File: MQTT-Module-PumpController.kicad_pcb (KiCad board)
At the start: 4 copper layers, 44 x 55.9 mm, 36 parts, among them IC801 LM5060MMX_NOPB, J301 A2541WV-10P, J302 A2541WV-10P, J303 1715721, J304 A2541HWV-3P, Q801 60V 38A, U201 ATtiny1614-SS

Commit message: Updated schematic and board with adjustments, updated board.
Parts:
- removed J304: A2541HWV-3P, CJT Connectors:PinSocket_1x03_P2.54mm_Vertical_Female
- removed R202: 4.7kΩ 1/8W 1%, JLCPCB Basic:RESC2013X65N
- removed R203: 33Ω 1/8W 1%, JLCPCB Basic:RESC2013X65N
- added R205: 220Ω 1/8W 1%, JLCPCB Basic:RESC2013X65N, F.Cu at (128.1, 77.7)
- added R206: 75Ω 1/8W 1%, JLCPCB Basic:RESC2013X65N, F.Cu at (123.7, 77.7)
- R201: value 33Ω 1/8W 1% -> 330Ω 1/8W 1%
- moved R201 15.5 mm to (125.5, 93.0), turned to 180 degrees
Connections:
- J301 pad 7: /Headers/CS -> /Controller/UPDI_C
- R201 pad 1: /Controller/P_WARN -> /Controller/UPDI
- R201 pad 2: Net-(D201-A) -> /Controller/UPDI_C
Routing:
- net +3V3: track 70.7 -> 58.1 mm
- net /Controller/UPDI: track 13.2 -> 22.2 mm
- net /Controller/UDPI_C: track 5.30 -> 0.00 mm
- net /Controller/UPDI_C: track 0.00 -> 5.30 mm
- net /Controller/PMP_EN: track 6.58 -> 8.93 mm
- net GND: vias 44 -> 48

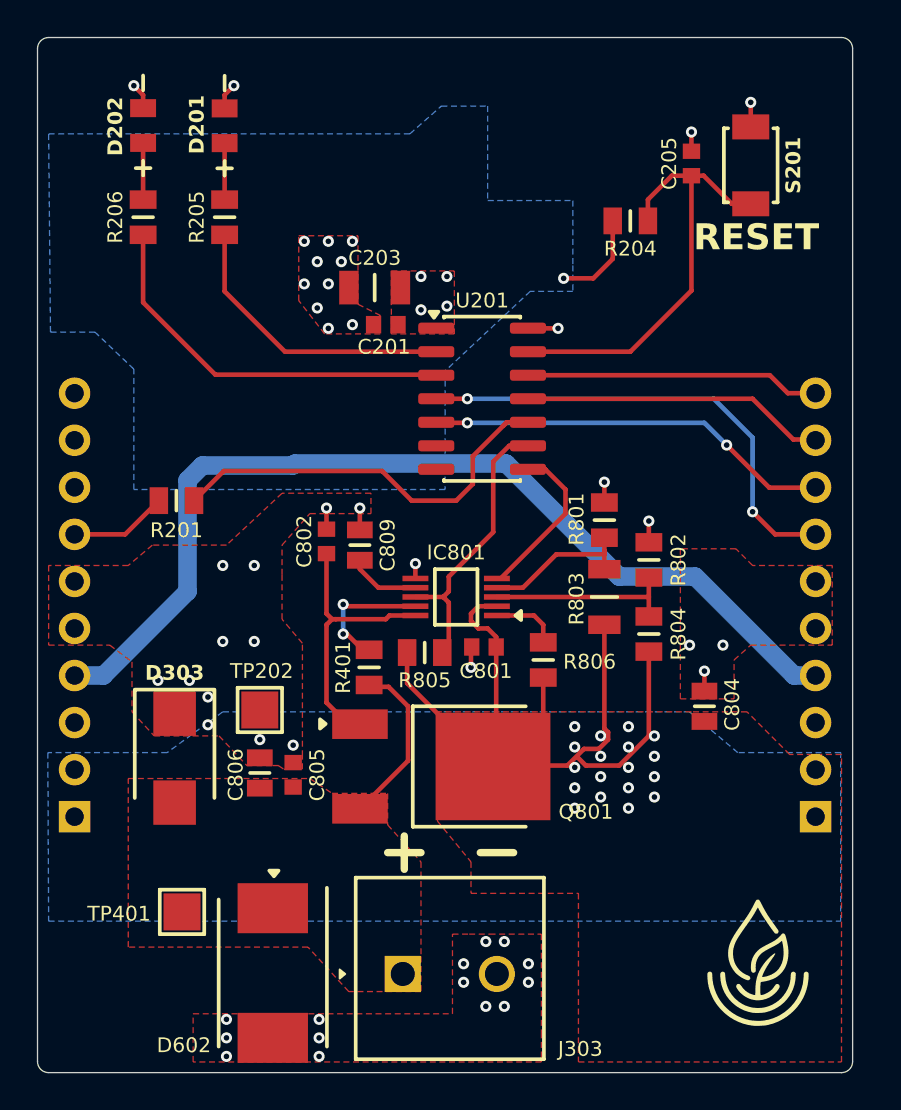
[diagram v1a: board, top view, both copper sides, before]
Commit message: Updated schematic, redesigned and included pump pressure switch. Regenerated all outputs.
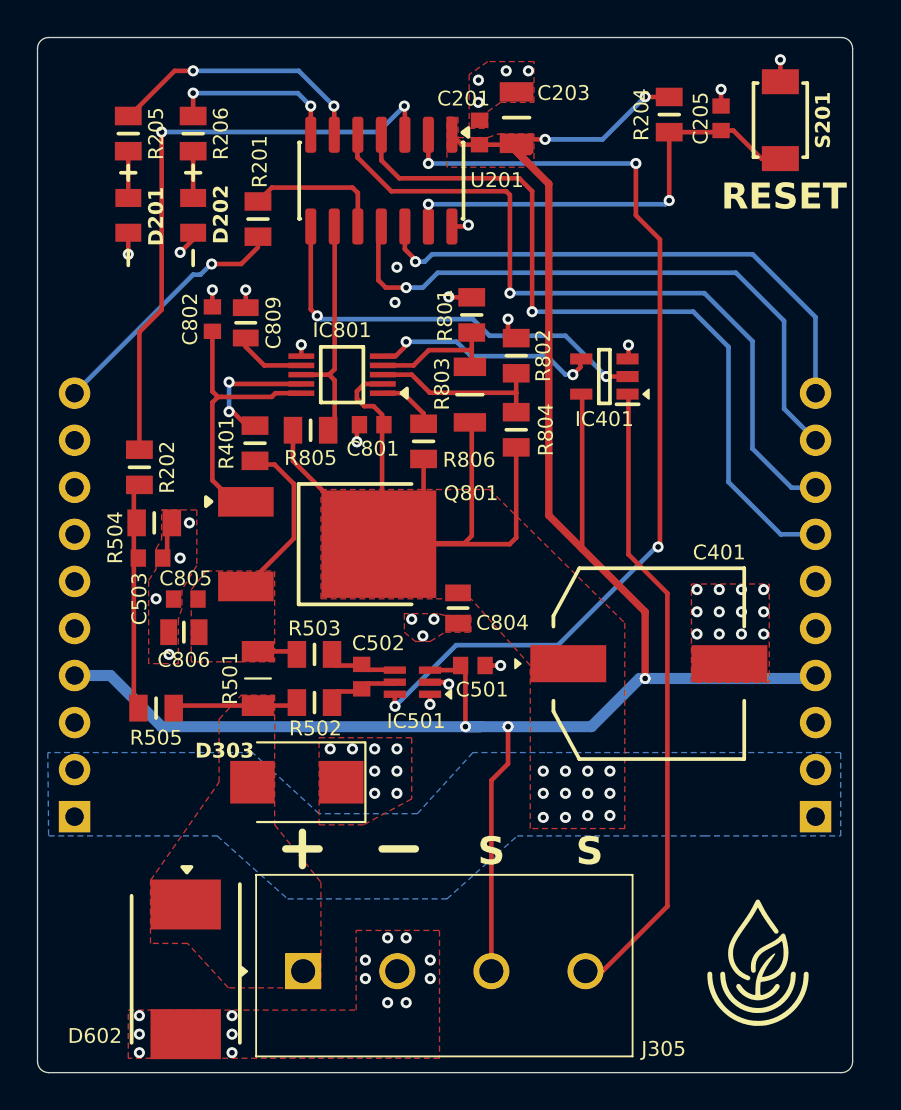
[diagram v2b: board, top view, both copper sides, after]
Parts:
- removed J303: 1715721, PHOENIX CONTACT Terminals:1715721
- removed TP202, TP401: TestPoint, TestPoint:TestPoint_Pad_2.0x2.0mm
- added C401: 470uF 20% 25V, PANASONIC Capacitors:EEEFK1V331P, F.Cu at (151.0, 101.8)
- added C501: 0.1uF 10% 50V, JLCPCB Basic:CAPC1608X90N, F.Cu at (141.5, 101.9)
- added C502: 22nF 10% 50V, JLCPCB Basic:CAPC1608X90N, F.Cu at (135.5, 102.5)
- added C503: 0.1uF 10% 50V, JLCPCB Basic:CAPC1608X90N, F.Cu at (124.1, 96.1)
- added IC401: SN74LVC1G08DBVR, TEXAS INSTRUMENTS ICs:SOT95P280X145-5N, F.Cu at (148.6, 86.3)
- added IC501: INA186A1IDCKR, TEXAS INSTRUMENTS ICs:SOT65P210X110-6N, F.Cu at (138.2, 102.8)
- added J305: 1715747, PHOENIX CONTACT Terminals:1715747, F.Cu at (132.3, 118.4)
- added R202: 1kΩ 1/8W 1%, JLCPCB Basic:RESC2013X65N, F.Cu at (123.5, 91.2)
- added R501: 20mΩ 1% 1W, VISHAY INTERTECH Resistors:R_1206_3216Metric, F.Cu at (129.9, 102.6)
- added R502: 100Ω 1/8W 1%, JLCPCB Basic:RESC2013X65N, F.Cu at (132.9, 103.9)
- added R503: 100Ω 1/8W 1%, JLCPCB Basic:RESC2013X65N, F.Cu at (132.9, 101.3)
- added R504: 24kΩ 1/8W 1%, JLCPCB Basic:RESC2013X65N, F.Cu at (124.3, 94.2)
- added R505: 100kΩ 1/8W 1%, JLCPCB Basic:RESC2013X65N, F.Cu at (124.4, 104.2)
- moved R201 15.8 mm to (129.9, 77.8), turned to -90 degrees
- moved C804 14.3 mm to (140.7, 98.8), turned to -90 degrees
- moved R401 13.6 mm to (129.7, 89.9)
- moved C802 13.5 mm to (127.4, 83.2)
- moved C809 13.5 mm to (129.2, 83.4)
- moved IC801 13.5 mm to (134.4, 86.2)
- moved Q801 13.5 mm to (138.2, 95.3)
- moved R805 13.5 mm to (132.7, 89.2)
- moved R806 13.5 mm to (138.8, 89.8)
- moved C801 13.4 mm to (136.0, 88.9)
- moved R801 13.2 mm to (141.4, 83.0)
- moved R802 13.1 mm to (143.8, 85.2)
- moved R804 13.1 mm to (143.8, 89.2)
- moved R803 13.1 mm to (141.3, 87.3)
- moved U201 13.0 mm to (136.6, 75.7), turned to -90 degrees
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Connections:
- C805 pad 1: /Headers/PMP+ -> /Pump Controller/PMP_Sense
- C806 pad 1: /Headers/PMP+ -> /Pump Controller/PMP_Sense
- IC801 pad 5: /Controller/PMP_EN -> Net-(IC401-Y)
- J301 pad 10: /Headers/MOSI -> /Controller/UPDI_C
- J301 pad 7: /Controller/UPDI_C -> /Headers/CS
- Q801 pad 3: /Headers/PMP+ -> /Pump Controller/PMP_Sense
- R401 pad 2: /Headers/PMP+ -> /Pump Controller/PMP_Sense
- U201 pad 2: /Controller/P_WARN -> /Controller/PI_SNS
- U201 pad 3: /Controller/P_ON -> /Controller/PV_SNS
- U201 pad 6: unconnected-(U201-PB3-Pad6) -> /Controller/P_WARN
- U201 pad 7: unconnected-(U201-PB2-Pad7) -> /Controller/P_ON
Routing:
- net +3V3: track 58.1 -> 116.6 mm
- net /Controller/PI_SNS: track 0.00 -> 52.3 mm, vias 0 -> 4
- net /Headers/Pressure_Sensor: track 0.00 -> 34.4 mm
- net /Controller/PV_SNS: track 0.00 -> 32.9 mm, vias 0 -> 2
- net /Controller/SNS: track 21.9 -> 39.9 mm, vias 2 -> 1
- net /Controller/SDA: track 16.5 -> 33.6 mm, vias 0 -> 1
- net /Controller/MOD: track 25.9 -> 41.3 mm, vias 2 -> 1
- net /Controller/UPDI: track 22.2 -> 7.63 mm
- net /Controller/PMP_EN: track 8.93 -> 23.1 mm, vias 0 -> 2
- net /Controller/SCL: track 16.2 -> 29.7 mm, vias 0 -> 1
- net /Controller/PV_SNS_R: track 0.00 -> 12.8 mm
- net Net-(IC401-Y): track 0.00 -> 12.5 mm, vias 0 -> 2
- net /Controller/P_ON: track 21.1 -> 9.43 mm, vias 0 -> 2
- net /Pump Controller/PMP_Sense: track 0.00 -> 11.4 mm
- net /Controller/UPDI_C: track 5.30 -> 13.2 mm, vias 0 -> 1
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- added copper zone on F.Cu, net /Pump Controller/PMP_Sense
- removed copper zone on B.Cu, net +3V3
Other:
- board text added: "Pressure Sensor"
- board text added: "Pump - / +"
- board text added: "S"

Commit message: Added pull downs on enable lines and regenerated outputs.
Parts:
- added R402: 10kΩ 1/8W 1%, JLCPCB Basic:RESC2013X65N, F.Cu at (152.4, 89.6)
- added R403: 10kΩ 1/8W 1%, JLCPCB Basic:RESC2013X65N, F.Cu at (152.4, 85.1)
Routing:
- net /Headers/Pressure_Sensor: track 34.4 -> 38.4 mm
- net /Controller/PMP_EN: track 23.1 -> 26.8 mm
- net /Controller/PI_SNS: track 52.3 -> 55.9 mm
- net GND: track 16.7 -> 19.3 mm, vias 62 -> 64

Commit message: Swapped 12v pull up to 3.3v pull up and added 0.1uf cap to AND, then regenerated outputs.
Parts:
- removed R805: 4.7kΩ 1/8W 1%, JLCPCB Basic:RESC2013X65N
- added C402: 0.1uF 10% 50V, JLCPCB Basic:CAPC1608X90N, F.Cu at (148.1, 89.0)
- added R404: 1kΩ 1/8W 1%, JLCPCB Basic:RESC2013X65N, F.Cu at (135.0, 83.1)
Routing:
- net +3V3: track 116.6 -> 134.5 mm, vias 5 -> 6
- net +12V: track 48.6 -> 40.6 mm
- net /Controller/PMP_Status: track 12.9 -> 9.63 mm
- net GND: track 19.3 -> 20.4 mm, vias 64 -> 65

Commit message: Updated layout, and regenerated outputs.
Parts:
- removed R201: 330Ω 1/8W 1%, JLCPCB Basic:RESC2013X65N
- added J303: A2541HWV-3P, CJT Connectors:PinSocket_1x03_P2.54mm_Vertical_Female, F.Cu at (159.6, 77.6)
- added R203: 470Ω 1/8W 1%, JLCPCB Basic:RESC2013X65N, F.Cu at (130.1, 73.9)
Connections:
- J301 pad 10: /Controller/UPDI_C -> /Headers/MOSI
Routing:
- net /Controller/UPDI_C: track 13.2 -> 32.9 mm, vias 1 -> 0
- net +3V3: track 134.5 -> 150.8 mm
- net /Controller/RESET: track 24.3 -> 23.3 mm
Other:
- board text added: "G"
- board text added: "U"
- board text added: "V"
